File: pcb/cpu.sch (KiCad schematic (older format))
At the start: 36 parts

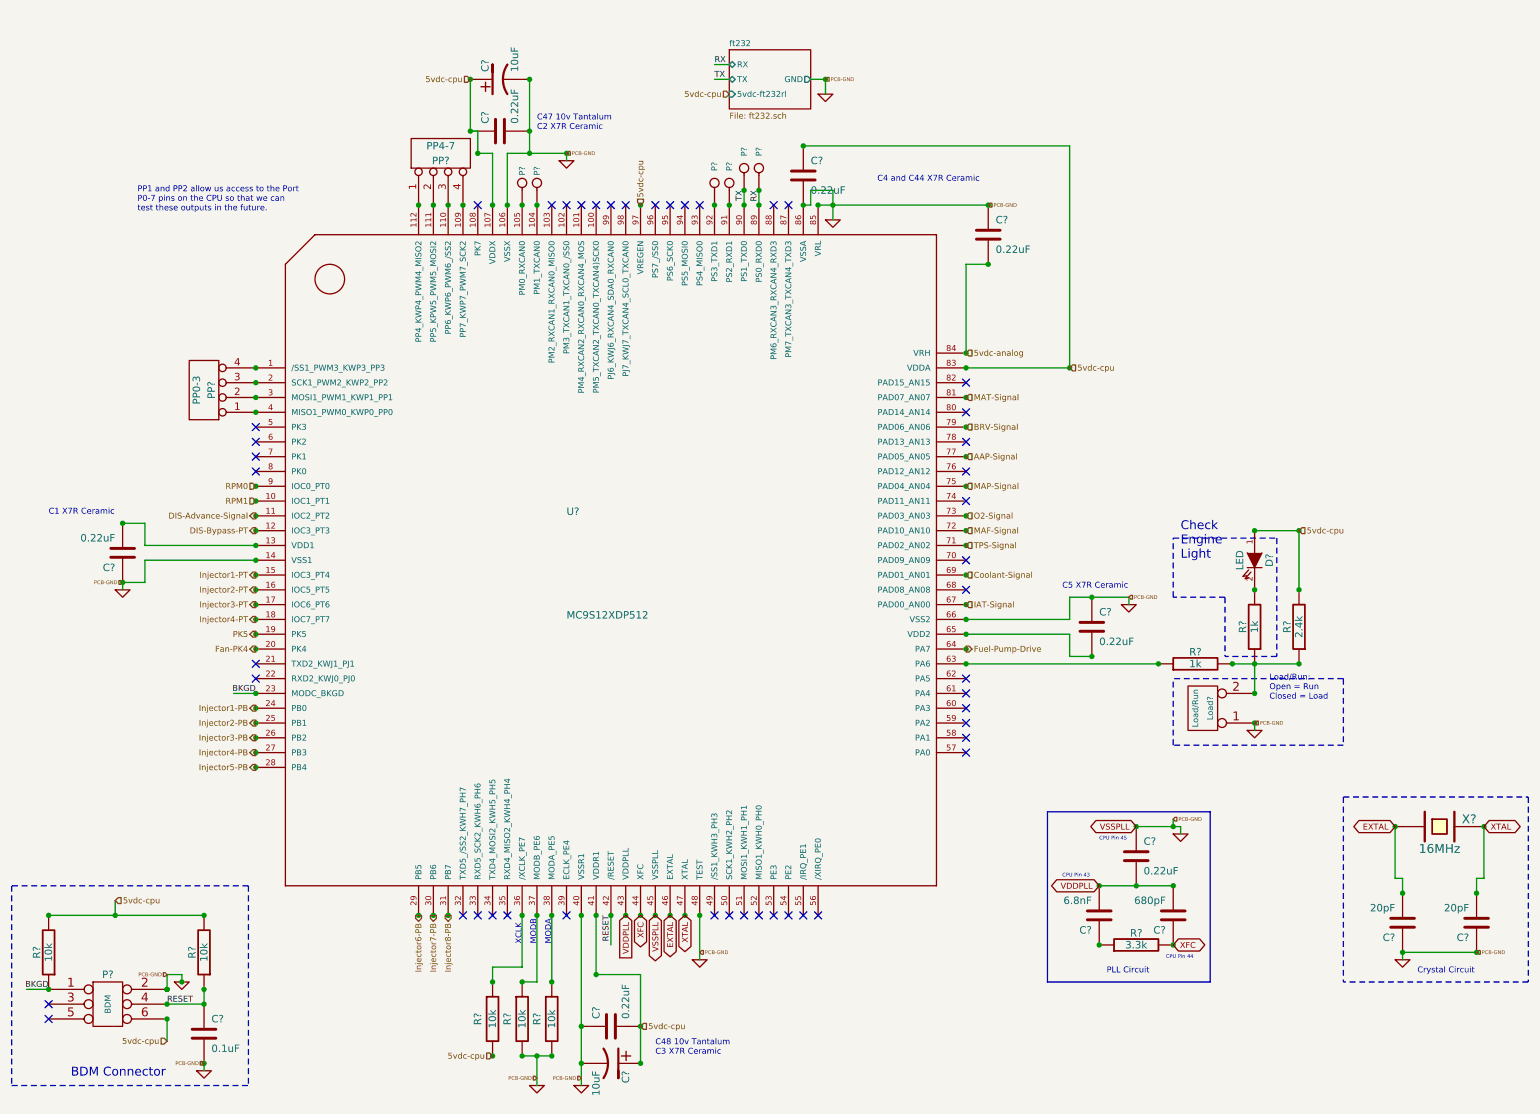
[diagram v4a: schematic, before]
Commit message: Changed fuel pump LSD out for high side driver, removed Fan and LSD1 individual low side drivers for a pair of dual MOSFET low side drivers.
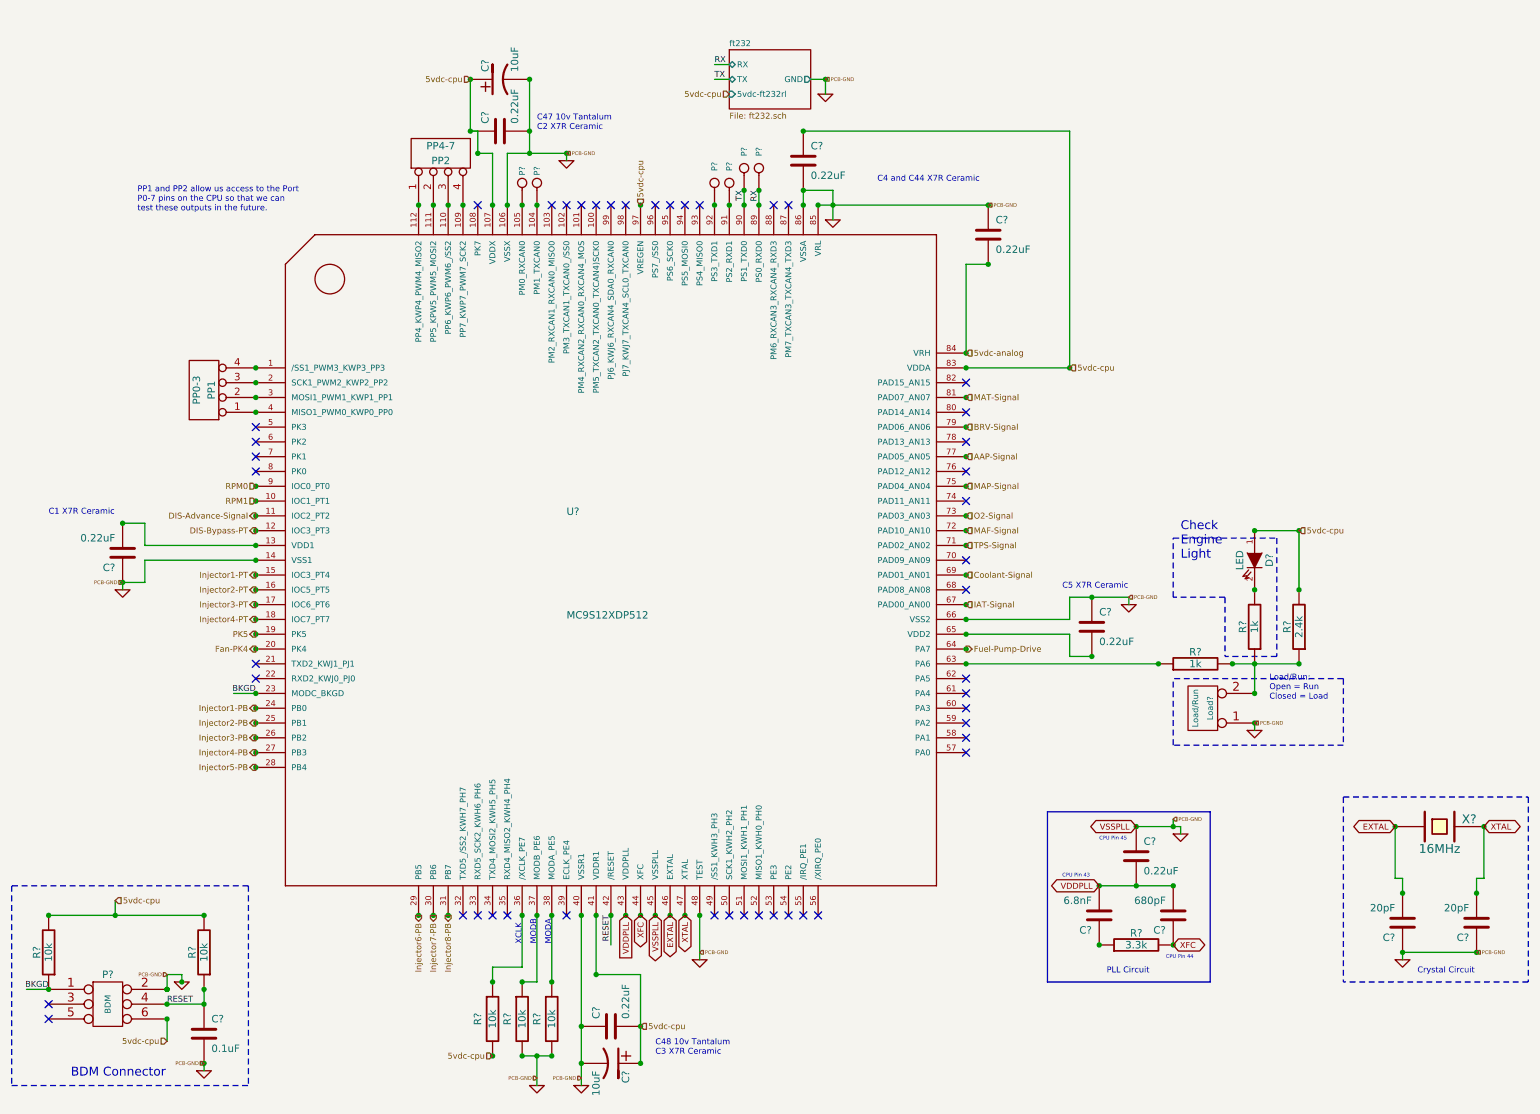
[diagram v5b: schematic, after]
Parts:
- gave numbers to parts that had none: 2
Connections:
- wire segments 82 -> 95
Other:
- moved on the sheet: C?
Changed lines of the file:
@@
 	4300 1450 4300 1400
 Wire Wire Line
-	4050 1400 4050 900
+	4050 1400 4050 1250
+Wire Wire Line
+	4050 1250 4050 900
 Wire Wire Line
 	4100 7700 4100 7500
@@
 Connection ~ 4800 7550
 Wire Wire Line
-	4800 7550 4800 6950
+	4800 7550 4800 7300
+Wire Wire Line
+	4800 7300 4800 6950
 Connection ~ 4500 6950
 Wire Wire Line
@@
 	7700 4550 7700 4400
 Wire Wire Line
-	7700 4400 8100 4400
+	7700 4400 7850 4400
+Wire Wire Line
+	7850 4400 8100 4400
 Wire Wire Line
 	1300 3900 1450 3900
@@
 	8450 6000 8450 5950
 Wire Wire Line
-	8450 5950 8150 5950
+	8450 5950 8400 5950
+Wire Wire Line
+	8400 5950 8150 5950
 Wire Wire Line
 	1850 7550 1850 7600
 Connection ~ 4050 1400
 Wire Wire Line
-	4400 6550 4400 7700
+	4400 6550 4400 7300
+Wire Wire Line
+	4400 7300 4400 7550
+Wire Wire Line
+	4400 7550 4400 7700
 Wire Wire Line
 	4500 6950 4500 6550
@@
 Connection ~ 1600 7050
 Wire Wire Line
-	7900 6350 8400 6350
+	7900 6350 8150 6350
+Wire Wire Line
+	8150 6350 8400 6350
 Wire Wire Line
 	10450 6300 10450 6400
@@
 Connection ~ 800  6550
 Wire Wire Line
-	1850 6550 800  6550
+	1850 6550 1250 6550
+Wire Wire Line
+	1250 6550 800  6550
 Wire Notes Line
 	9550 5750 9550 7000
@@
 	6050 900  5950 900
 Wire Wire Line
-	7700 2850 7700 1350
-Wire Wire Line
-	7700 1350 5900 1350
+	7700 2850 7700 1250
+Wire Wire Line
+	7700 1250 5900 1250
 Wire Wire Line
 	7000 2750 7000 2150
@@
 	7000 2150 7150 2150
 Connection ~ 7150 1750
-Connection ~ 5900 1350
+Connection ~ 5900 1250
 Connection ~ 7150 2150
 Connection ~ 9250 3950
@@
 	4200 6550 4200 7000
 Wire Wire Line
-	4200 7500 4000 7500
+	4200 7500 4100 7500
+Wire Wire Line
+	4100 7500 4000 7500
 Wire Wire Line
 	4000 6550 4000 6900
@@
 	9100 4800 8750 4800
 Wire Wire Line
-	8800 4850 9250 4850
+	8800 4850 8950 4850
+Wire Wire Line
+	8950 4850 9250 4850
 Connection ~ 8800 4850
 Connection ~ 8300 4850
@@
 Connection ~ 8400 5950
 Wire Wire Line
-	5900 1750 5950 1750
-Wire Wire Line
-	5950 1750 5950 1650
-Wire Wire Line
-	5950 1650 6100 1650
-Wire Wire Line
-	6100 1650 6100 1850
-Wire Wire Line
-	7150 1750 6000 1750
+	5900 1750 5900 1750
+Wire Wire Line
+	5900 1750 5900 1650
+Wire Wire Line
+	5900 1650 6100 1650
+Wire Wire Line
+	6100 1650 6100 1750
+Wire Wire Line
+	6100 1750 6100 1850
+Wire Wire Line
+	7150 1750 6100 1750
+Wire Wire Line
+	6100 1750 6000 1750
 Connection ~ 5400 1750
 Connection ~ 5300 1750
@@
 Connection ~ 2200 4650
 Wire Wire Line
-	3900 1400 4300 1400
+	3900 1400 4050 1400
+Wire Wire Line
+	4050 1400 4300 1400
 $Comp
 L CONN_1 P?
@@
 NoConn ~ 7000 4950
 $Comp
-L CONN_4 PP?
+L CONN_4 PP2
 U 1 1 4F221E2B
 P 3450 1400
-F 0 "PP?" V 3400 1400 50  0000 C CNN
+F 0 "PP2" V 3400 1400 50  0000 C CNN
 F 1 "PP4-7" V 3500 1400 50  0000 C CNN
 F 2 "" H 3450 1400 60  0001 C CNN
@@
 $EndComp
 $Comp
-L CONN_4 PP?
+L CONN_4 PP1
 U 1 1 4F221DE9
 P 1850 3000
-F 0 "PP?" V 1800 3000 50  0000 C CNN
+F 0 "PP1" V 1800 3000 50  0000 C CNN
 F 1 "PP0-3" V 1900 3000 50  0000 C CNN
 F 2 "" H 1850 3000 60  0001 C CNN
@@
 L C C?
 U 1 1 4F0A32B1
-P 5900 1550
-F 0 "C?" H 5950 1650 50  0000 L CNN
-F 1 "0.22uF" H 5950 1450 50  0000 L CNN
-F 2 "" H 5900 1550 60  0001 C CNN
-F 3 "" H 5900 1550 60  0001 C CNN
-	1    5900 1550
+P 5900 1450
+F 0 "C?" H 5950 1550 50  0000 L CNN
+F 1 "0.22uF" H 5950 1350 50  0000 L CNN
+F 2 "" H 5900 1450 60  0001 C CNN
+F 3 "" H 5900 1450 60  0001 C CNN
+	1    5900 1450
 	1    0    0    -1
 $EndComp
@@
 	0    -1   -1   0
 $EndComp
+Connection ~ 5900 1650
 $EndSCHEMATC

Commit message: Changed revision to 0.7-alpha and git hash to xxxxxxxxxx to show that this is in progress.
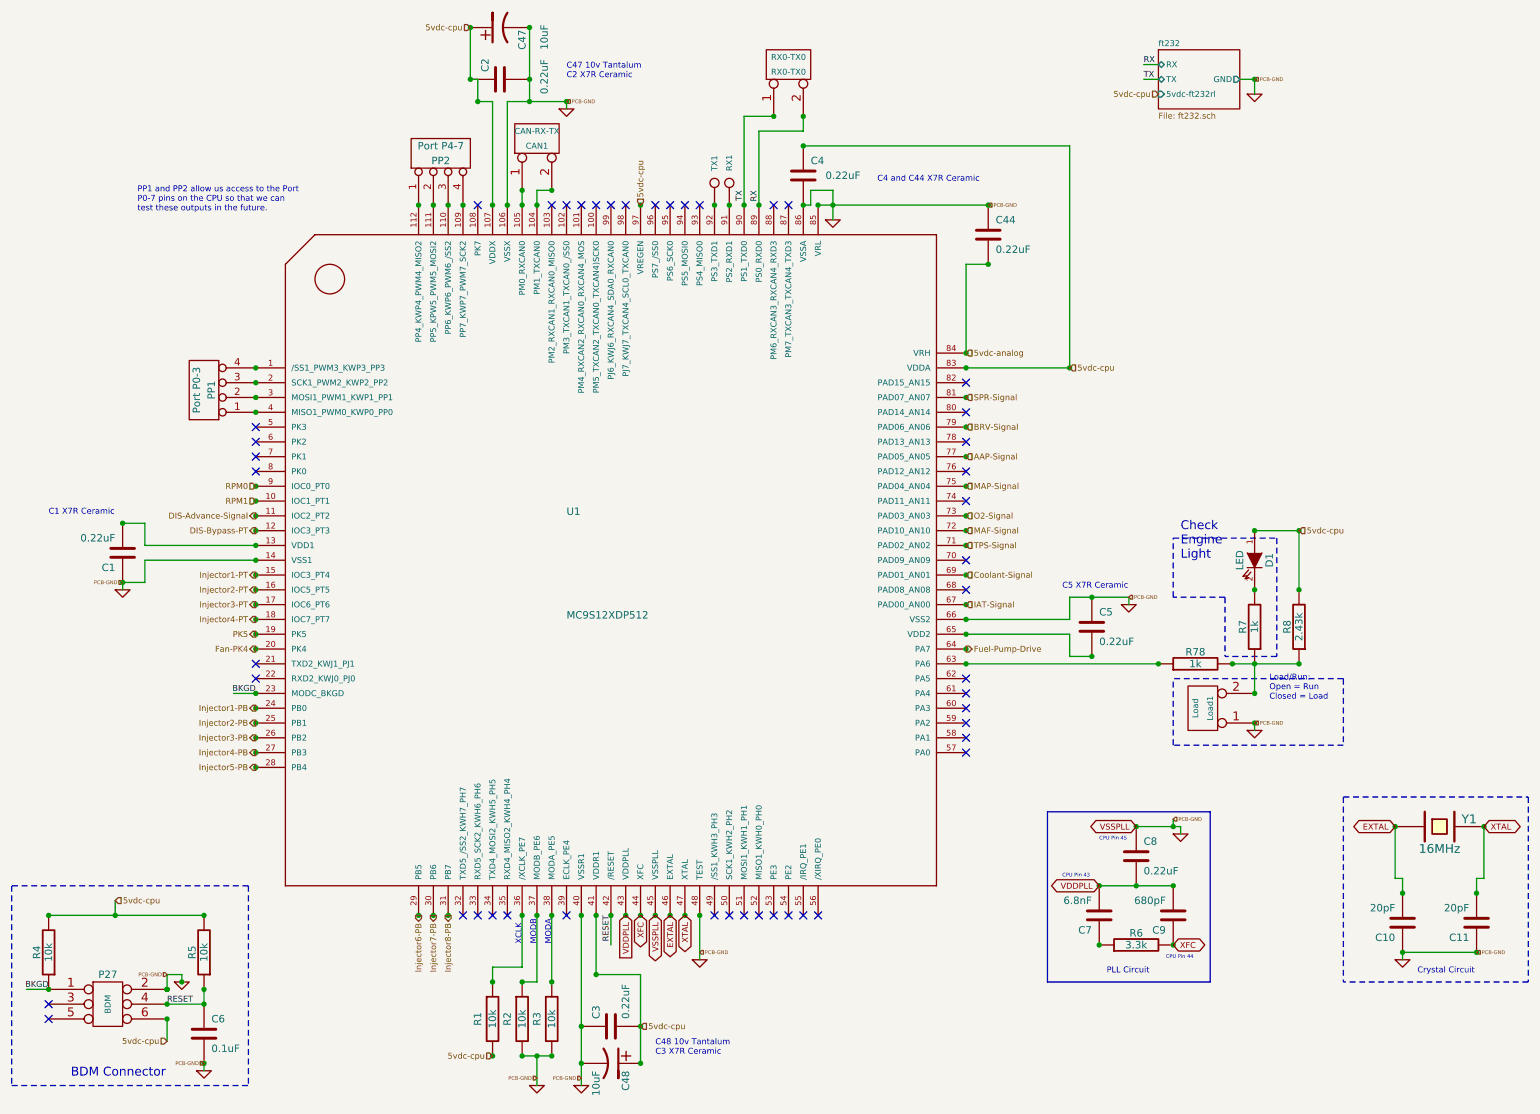
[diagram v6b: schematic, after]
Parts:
- removed P?: TX, symbol CONN_1
- removed P?: RX, symbol CONN_1
- removed P?: RXCAN0, symbol CONN_1
- removed P?: TXCAN0, symbol CONN_1
- added CAN1: CAN-RX-TX, symbol CONN_2
- added RX0-TX0: RX0-TX0, symbol CONN_2
- Load1: renamed from Load?; value Load/Run -> Load
- PP1: value PP0-3 -> Port P0-3
- PP2: value PP4-7 -> Port P4-7
- R8: renamed from R?; value 2.4k -> 2.43k
- gave numbers to parts that had none: 28
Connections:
- net labels added: SPR-Signal
- net labels removed: MAT-Signal
- wire segments 95 -> 88
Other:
- moved on the sheet: C2, C4, C47
